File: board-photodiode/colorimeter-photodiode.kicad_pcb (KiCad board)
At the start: 2 copper layers, 23.5 x 7.6 mm, 2 parts, among them J1 Conn_02x02_Counter_Clockwise

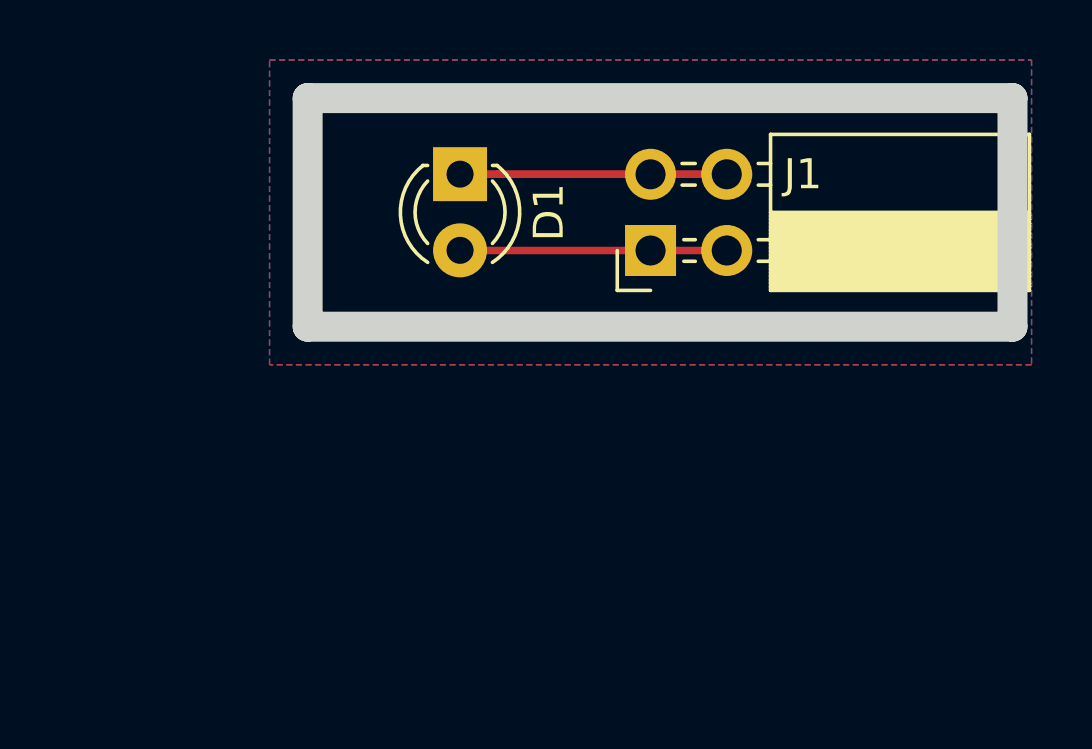
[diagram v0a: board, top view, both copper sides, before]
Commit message: Change PD, LED boards to match pinout on main board
Added ground connections to both
Changed Photodiode to have 3x2 connector
Changed LED to common anode
Added new symbol & footprint for common anode RGB LED

Signed-off-by: Ioan Dragomir <ioan.dragomir@analog.com>
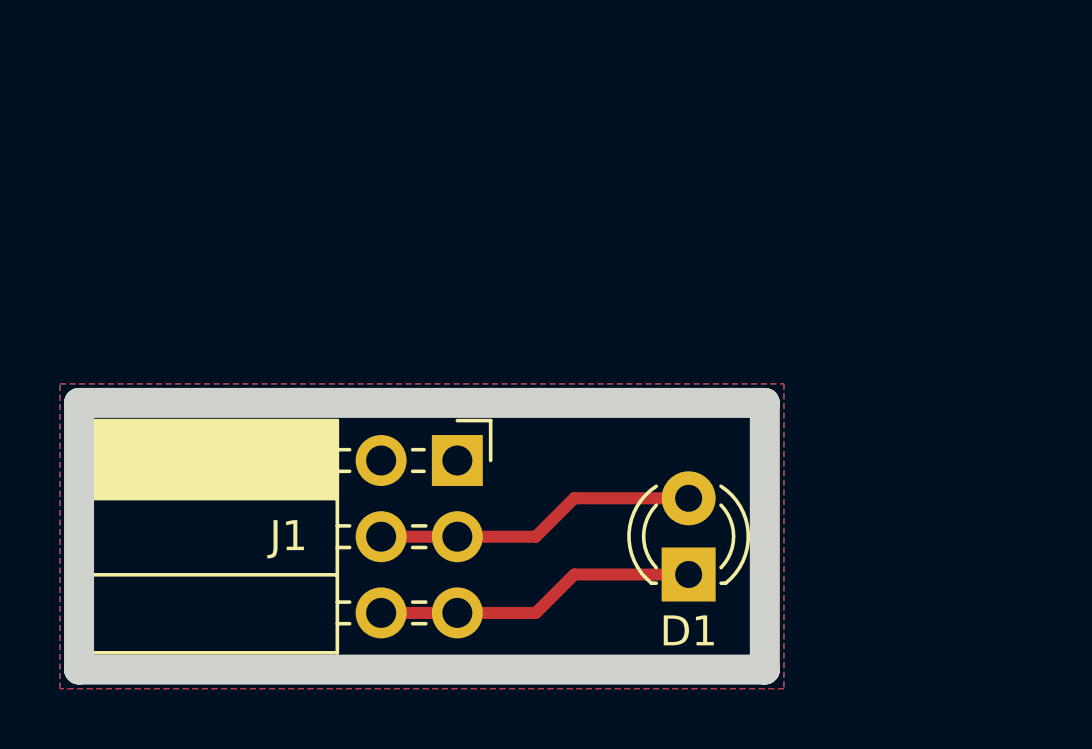
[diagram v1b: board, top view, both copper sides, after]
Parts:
- J1: value Conn_02x02_Counter_Clockwise -> Conn_02x03_Counter_Clockwise; footprint Connector_PinSocket_2.54mm:PinSocket_2x02_P2.54mm_Horizontal -> Connector_PinSocket_2.54mm:PinSocket_2x03_P2.54mm_Horizontal
- moved D1 15.4 mm to (102.9, 79.4), turned to 90 degrees
- moved J1 9.51 mm to (95.2, 75.6), turned to 0 degrees
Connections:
- J1 pad 1: Net-(D1-A) -> GND
- J1 pad 2: Net-(D1-K) -> Net-(D1-A)
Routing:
- net Net-(D1-A): track 8.89 -> 10.8 mm
- net Net-(D1-K): track 8.90 -> 10.8 mm
- added copper zone on B.Cu, net GND
- added copper zone on F.Cu, net GND
- removed copper zone on B.Cu, net (none)
- removed copper zone on F.Cu, net (none)
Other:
- board size 23.5 x 7.6 mm -> 22.9 x 8.9 mm

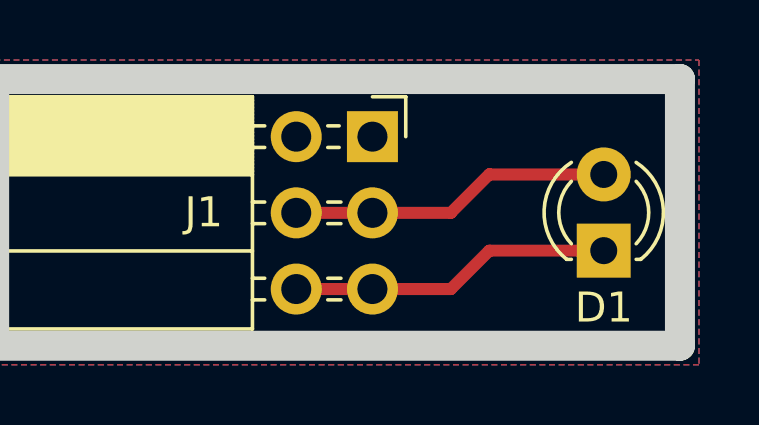
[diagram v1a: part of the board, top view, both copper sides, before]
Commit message: Reorder photodiode riser board pins
Signed-off-by: Ioan Dragomir <ioan.dragomir@analog.com>
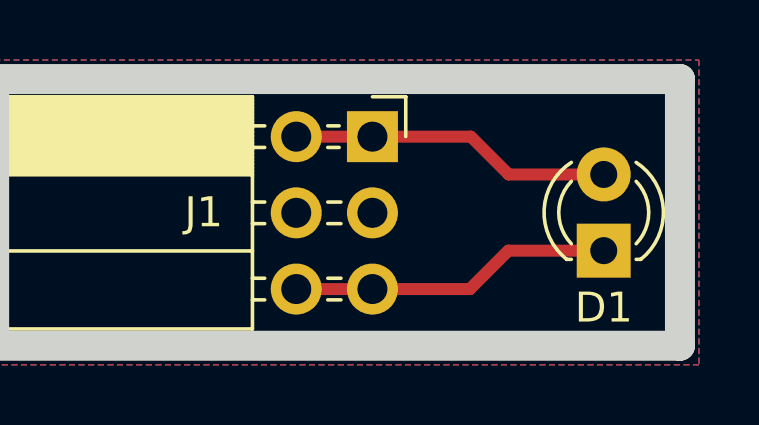
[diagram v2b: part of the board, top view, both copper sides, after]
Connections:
- J1 pad 1: GND -> Net-(D1-A)
- J1 pad 2: Net-(D1-A) -> GND
